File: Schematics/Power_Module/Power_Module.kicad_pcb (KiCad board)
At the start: 4 copper layers, 69.5 x 60 mm, 135 parts, among them J1 ScrewSwitch, J2 Battery, J3 ScrewSwitch, J4 GSE, J5 USB_C_Female_USB2_Small, J6 SWD_B, J7 Stack Male Edge Connector, Q1 AO4447A, Q2 TSM2309CX, Q3 DMN6040SSD-13, SW1 SW_STM_RESET, SW2 SW_STM_BOOT_MODE, U1 TPS61175PWPR, U10 LM66100DCKR, U11 LM66100DCKR, U12 AMS1117-3.3, U13 CP2102N-A02-GQFN20R, U14 STM32F103CBT6, U15 ISO1044BDR, U16 W25Q128JVS, U2 LM74700QDBVRQ1, U3 LM74700QDBVRQ1, U4 ACS37041KLHBLT-010B3, U5 ACS37041KLHBLT-010B5, U6 INA181A2, U7 LMR51430XDDCR, U8 LMR51430XDDCR, U9 LM66100DCKR, Y1 X322516MMB4SI

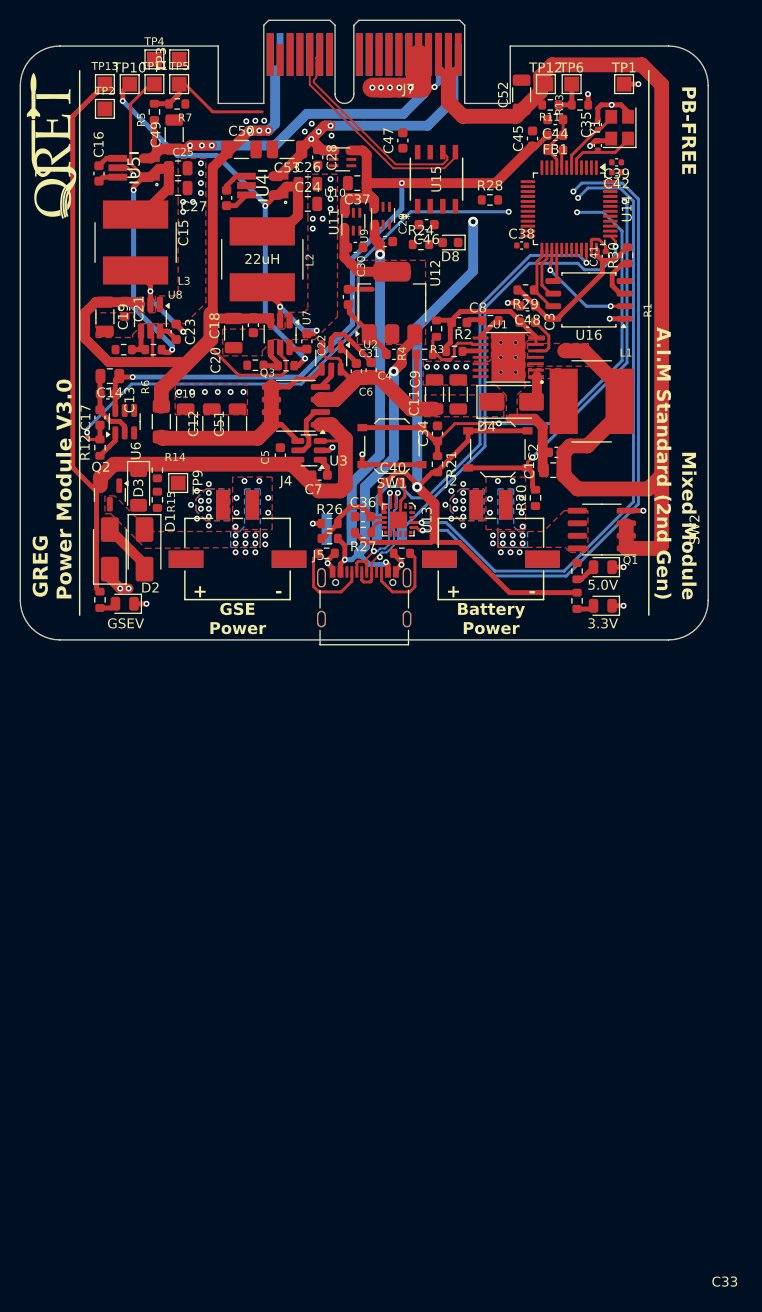
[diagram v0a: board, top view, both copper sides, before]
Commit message: finished all traces, confirmed major DRC errors  - need to fix silkscreen  - review needed and LCSC verification
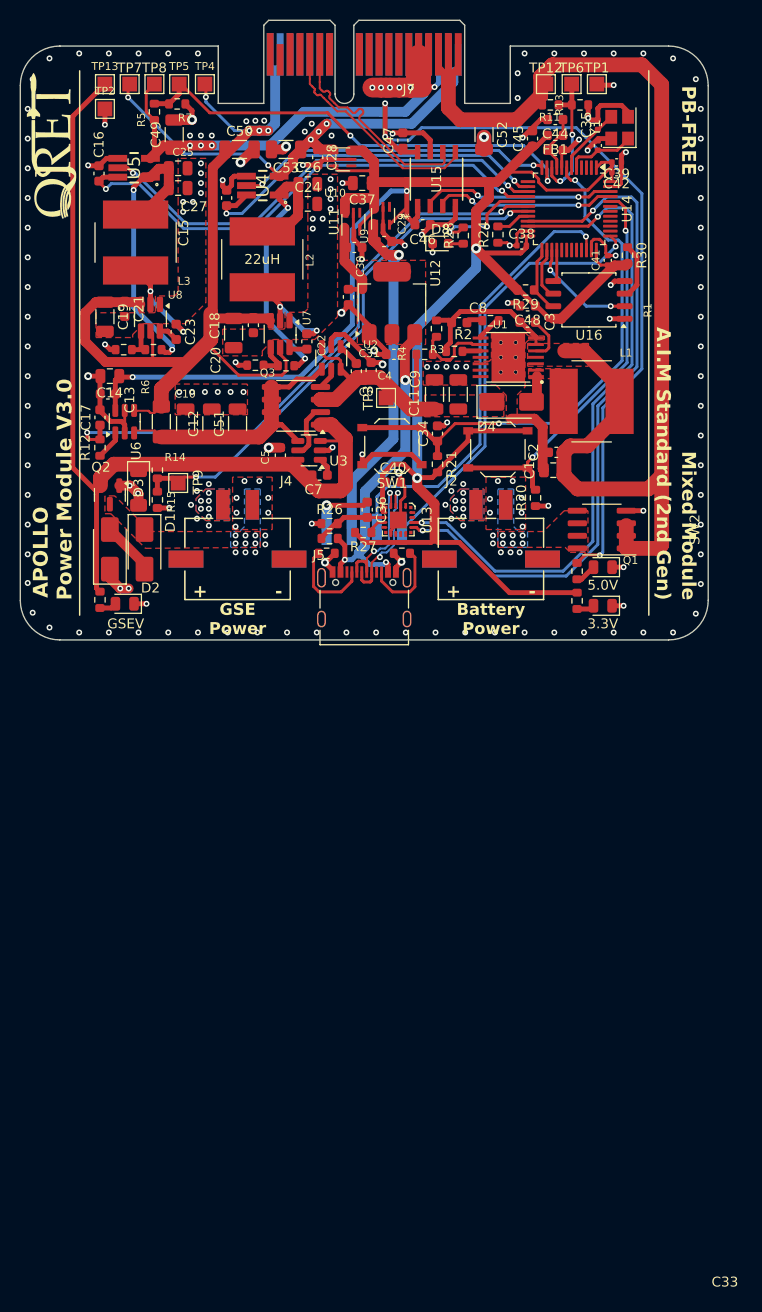
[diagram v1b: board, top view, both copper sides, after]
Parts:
- removed TP10: 3v3, TestPoint:TestPoint_Pad_1.5x1.5mm
- removed TP11: 5V, TestPoint:TestPoint_Pad_1.5x1.5mm
- added TP7: 3v3, TestPoint:TestPoint_Pad_1.5x1.5mm, F.Cu at (141.3, 43.6)
- added TP8: 5V, TestPoint:TestPoint_Pad_1.5x1.5mm, F.Cu at (143.8, 43.6)
- moved TP3 40.1 mm to (167.2, 75.3)
- moved R24 7.84 mm to (178.5, 58.8), turned to 90 degrees
- moved TP4 5.68 mm to (148.9, 43.6)
- moved C52 5.54 mm to (177.1, 48.7), turned to -90 degrees
- moved R28 4.50 mm to (175.0, 58.9), turned to 90 degrees
- moved TP1 2.75 mm to (188.5, 43.6)
- moved D8 1.00 mm to (172.7, 59.7), turned to 0 degrees
- moved C36 0.82 mm to (165.3, 86.6), turned to -90 degrees
- moved C37 0.50 mm to (164.8, 53.6)
- moved C41 0.47 mm to (189.6, 61.4)
- moved C46 0.40 mm to (170.9, 57.8)
- moved C50 0.20 mm to (152.4, 50.2)
- moved C29 0.10 mm to (167.0, 59.5)
- moved C30 0.10 mm to (164.0, 60.1)
- moved C53 0.10 mm to (157.1, 50.2)
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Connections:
- TP4 pad 1: 24V_MUX_Pre -> 24V_MUX
- U14 pad 12: 5V_ACS_PWR -> 3.3V_CURR_SENSE
- U14 pad 14: 3.3V_CURR_SENSE -> 3.3V_ACS_PWR
- U14 pad 16: 3.3V_ACS_PWR -> 5V_ACS_PWR
- U14 pad 18: GSE_SENSE -> 24V_CURR_SENSE
- U14 pad 19: 24V_CURR_SENSE -> GSE_SENSE
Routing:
- net GND: track 127.3 -> 214.5 mm, vias 88 -> 198
- net 5V_PSU: track 44.8 -> 125.3 mm, vias 3 -> 6
- net GSE_SENSE: track 0.00 -> 51.9 mm, vias 0 -> 2
- net 3.3V_MUX: track 177.8 -> 228.1 mm
- net 5V_ACS_PWR: track 2.07 -> 51.8 mm, vias 0 -> 2
- net 5V_CURR_SENSE: track 1.98 -> 47.7 mm, vias 1 -> 2
- net 3.3V_ACS_PWR: track 2.45 -> 38.3 mm, vias 0 -> 2
- net 5V_SENSE: track 13.4 -> 47.0 mm, vias 0 -> 2
- net 3.3V_CURR_SENSE: track 0.00 -> 32.0 mm, vias 0 -> 2
- net 3.3V_PSU_Pre: track 49.6 -> 27.5 mm, vias 3 -> 2
- net CAN_TX: track 0.00 -> 19.2 mm, vias 0 -> 2
- net CAN_RX: track 0.00 -> 18.0 mm, vias 0 -> 2
- net 3.3V_PSU: track 34.1 -> 49.9 mm, vias 3 -> 5
- net 5V_PSU_Pre: track 42.0 -> 29.5 mm
- net DB_LED: track 0.00 -> 11.5 mm, vias 0 -> 2
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- added copper zone on In1.Cu, net GND
- added copper zone on In2.Cu, net GND
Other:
- board text added: "APOLLO"
- board text removed: "GREG"
